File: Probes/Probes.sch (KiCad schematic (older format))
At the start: 40 parts, among them IC1 ADUM1251ARZ, J1 Conn_Coaxial, J2 Conn_01x02_Male, J3 Conn_01x05_Male, J4 Conn_01x05_Male, U1 LMC6042IN, U3 ADS1014IDGS

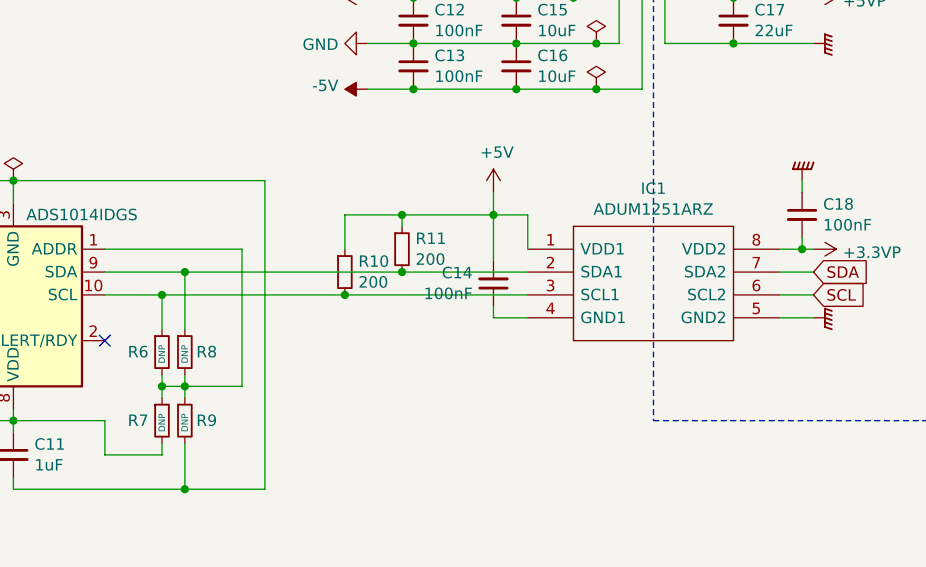
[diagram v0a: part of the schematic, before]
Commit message: invert ADUM1251 invert J3
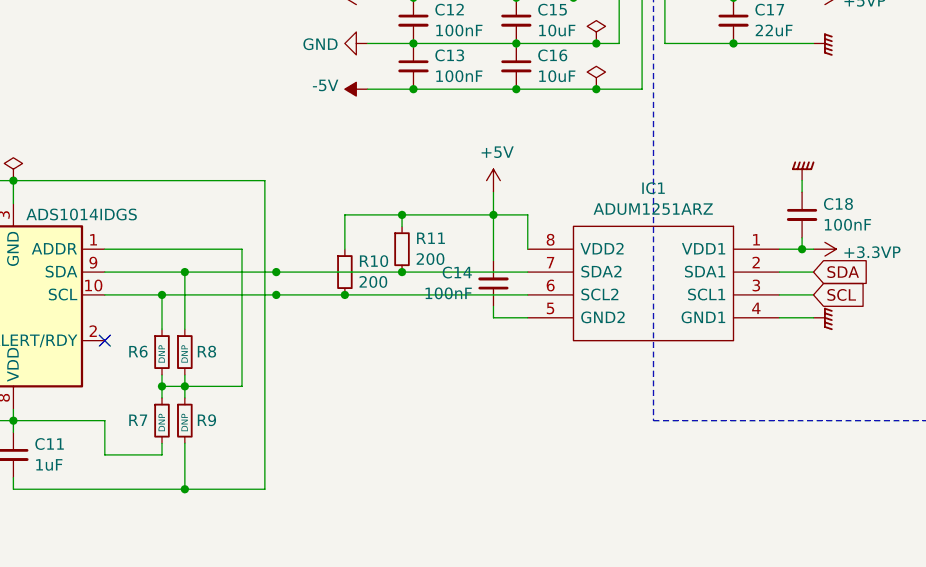
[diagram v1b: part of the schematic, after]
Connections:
- net +3.3VP: now also IC1.1 (VDD1); no longer IC1.8 (VDD2)
- net +5V: now also IC1.8 (VDD2); no longer IC1.1 (VDD1)
- net GNDPWR: now also IC1.4 (GND1); no longer IC1.5 (GND2)
- net SCL: now also IC1.3 (SCL1); no longer IC1.6 (SCL2)
- net SDA: now also IC1.2 (SDA1); no longer IC1.7 (SDA2)
- net at R11.2, R8.1, U3.9 (SDA): now also IC1.7 (SDA2); no longer IC1.2 (SDA1)
- net at R10.2, R6.1, U3.10 (SCL): now also IC1.6 (SCL2); no longer IC1.3 (SCL1)
- net at C14.1: now also IC1.5 (GND2); no longer IC1.4 (GND1)
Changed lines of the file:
@@
 L archive:SamacSys_Parts_ADUM1251ARZ IC1
 U 1 1 621EB135
-P 7950 2950
-F 0 "IC1" H 8500 3215 50  0000 C CNN
-F 1 "ADUM1251ARZ" H 8500 3124 50  0000 C CNN
-F 2 "SamacSys_Parts:SOIC127P600X175-8N" H 8900 3050 50  0001 L CNN
-F 3 "https://datasheet.datasheetarchive.com/originals/distributors/Datasheets-DGA3/264898.pdf" H 8900 2950 50  0001 L CNN
-F 4 "Hot Swappable, Dual I2C Isolators" H 8900 2850 50  0001 L CNN "Description"
-F 5 "1.75" H 8900 2750 50  0001 L CNN "Height"
-F 6 "Analog Devices" H 8900 2650 50  0001 L CNN "Manufacturer_Name"
-F 7 "ADUM1251ARZ" H 8900 2550 50  0001 L CNN "Manufacturer_Part_Number"
-F 8 "584-ADUM1251ARZ" H 8900 2450 50  0001 L CNN "Mouser Part Number"
-F 9 "https://www.mouser.co.uk/ProductDetail/Analog-Devices/ADUM1251ARZ?qs=WIvQP4zGani5W7Ldr0QsZA%3D%3D" H 8900 2350 50  0001 L CNN "Mouser Price/Stock"
-F 10 "ADUM1251ARZ" H 8900 2250 50  0001 L CNN "Arrow Part Number"
-F 11 "https://www.arrow.com/en/products/adum1251arz/analog-devices?region=nac" H 8900 2150 50  0001 L CNN "Arrow Price/Stock"
-	1    7950 2950
-	1    0    0    -1
+P 9050 2950
+F 0 "IC1" H 9600 3215 50  0000 C CNN
+F 1 "ADUM1251ARZ" H 9600 3124 50  0000 C CNN
+F 2 "SamacSys_Parts:SOIC127P600X175-8N" H 10000 3050 50  0001 L CNN
+F 3 "https://datasheet.datasheetarchive.com/originals/distributors/Datasheets-DGA3/264898.pdf" H 10000 2950 50  0001 L CNN
+F 4 "Hot Swappable, Dual I2C Isolators" H 10000 2850 50  0001 L CNN "Description"
+F 5 "1.75" H 10000 2750 50  0001 L CNN "Height"
+F 6 "Analog Devices" H 10000 2650 50  0001 L CNN "Manufacturer_Name"
+F 7 "ADUM1251ARZ" H 10000 2550 50  0001 L CNN "Manufacturer_Part_Number"
+F 8 "584-ADUM1251ARZ" H 10000 2450 50  0001 L CNN "Mouser Part Number"
+F 9 "https://www.mouser.co.uk/ProductDetail/Analog-Devices/ADUM1251ARZ?qs=WIvQP4zGani5W7Ldr0QsZA%3D%3D" H 10000 2350 50  0001 L CNN "Mouser Price/Stock"
+F 10 "ADUM1251ARZ" H 10000 2250 50  0001 L CNN "Arrow Part Number"
+F 11 "https://www.arrow.com/en/products/adum1251arz/analog-devices?region=nac" H 10000 2150 50  0001 L CNN "Arrow Price/Stock"
+	1    9050 2950
+	-1   0    0    -1
 $EndComp
 $Comp
@@
 Connection ~ 6350 3150
 Wire Wire Line
-	6350 3150 7150 3150
+	6350 3150 6850 3150
 Wire Wire Line
 	6450 3300 6450 3050
 Connection ~ 6450 3050
 Wire Wire Line
-	6450 3050 7400 3050
+	6450 3050 6850 3050
 Wire Wire Line
 	5700 2750 5700 2650
@@
 	1    0    0    -1
 $EndComp
+Connection ~ 6850 3150
+Wire Wire Line
+	6850 3150 7150 3150
+Connection ~ 6850 3050
+Wire Wire Line
+	6850 3050 7400 3050
 $EndSCHEMATC

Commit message: missing gnd missing pull up resistor on DC/DC
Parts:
- added J5, J6, J7, J8: Conn_01x01_Female, Connector_PinSocket_2.00mm:PinSocket_1x01_P2.00mm_Vertical, symbol archive:Connector_Conn_01x01_Female
- added R12, R13: 2700, Resistor_SMD:R_0805_2012Metric_Pad1.20x1.40mm_HandSolder, symbol archive:Device_R_Small
- added R14, R15: 560, Resistor_SMD:R_0805_2012Metric_Pad1.20x1.40mm_HandSolder, symbol archive:Device_R_Small
- C10, C5: value 100nF -> DNP
- C3: value 1uF -> 47nF DNP
- R10, R11: value 200 -> 2700
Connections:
- wire segments 168 -> 184
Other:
- note added: "Va=Vsonde*( 1 + R2/R1)"
- note removed: "Va=Vsonde*( 1 + R3/R2)"
- moved on the sheet: C12, C13, C15, C16

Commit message: horizontal connector
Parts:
- J3, J4: footprint Connector_JST:JST_PH_B5B-PH-K_1x05_P2.00mm_Vertical -> Connector_JST:JST_PH_S5B-PH-K_1x05_P2.00mm_Horizontal
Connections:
- wire segments 184 -> 183
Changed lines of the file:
@@
 F 0 "J3" H 10922 1028 50  0000 R CNN
 F 1 "Conn_01x05_Male" H 10922 983 50  0001 R CNN
-F 2 "Connector_JST:JST_PH_B5B-PH-K_1x05_P2.00mm_Vertical" H 10950 1050 50  0001 C CNN
+F 2 "Connector_JST:JST_PH_S5B-PH-K_1x05_P2.00mm_Horizontal" H 10950 1050 50  0001 C CNN
 F 3 "~" H 10950 1050 50  0001 C CNN
 	1    10950 1050
@@
 F 0 "J4" H 10922 1678 50  0000 R CNN
 F 1 "Conn_01x05_Male" H 10922 1633 50  0001 R CNN
-F 2 "Connector_JST:JST_PH_B5B-PH-K_1x05_P2.00mm_Vertical" H 10950 1700 50  0001 C CNN
+F 2 "Connector_JST:JST_PH_S5B-PH-K_1x05_P2.00mm_Horizontal" H 10950 1700 50  0001 C CNN
 F 3 "~" H 10950 1700 50  0001 C CNN
 	1    10950 1700
@@
 Wire Wire Line
 	3500 4400 3500 4550
-Wire Wire Line
-	3500 4550 3000 4550
 Connection ~ 2000 4550
 Wire Wire Line
@@
 	0    1    1    0
 $EndComp
-Connection ~ 3000 4550
-Wire Wire Line
-	3000 4550 2700 4550
 Connection ~ 3150 1600
 Wire Wire Line
 	3150 1600 3500 1600
+Wire Wire Line
+	2700 4550 3500 4550
 $EndSCHEMATC
